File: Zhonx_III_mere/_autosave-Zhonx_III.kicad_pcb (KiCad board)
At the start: 2 copper layers, 70 x 97 mm, 133 parts, among them K1 L_Motor, K2 R_Motor, K3 USART, P1 JTAG, Q1 FDV301N, Q2 FDV301N, U1 MCP73213, U10 BSL214N, U11 BSL214N, U12 24LC64T, U14 STM32F405RGT6, U16 Line_1, U17 Line_2, U18 Line_3, U19 Line_4, U2 A3918, U20 Line_5, U3 A3918, U4 LTC2955CTS8-2, U5 SIB911DK, U6 SI1551DL, U7 LM2940, U8 MCP1700, U9 MCP1700, X1 16MHz

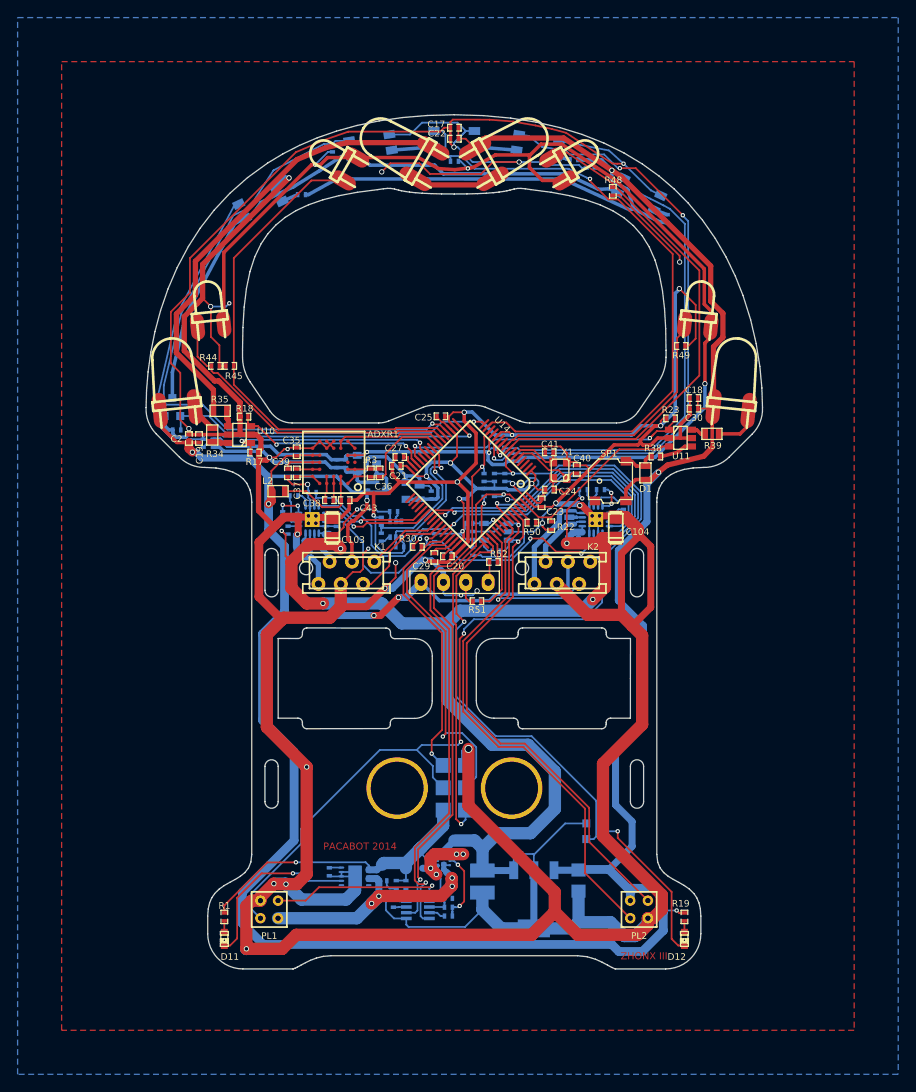
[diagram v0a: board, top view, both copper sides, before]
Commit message: Create Zhonx mere V2
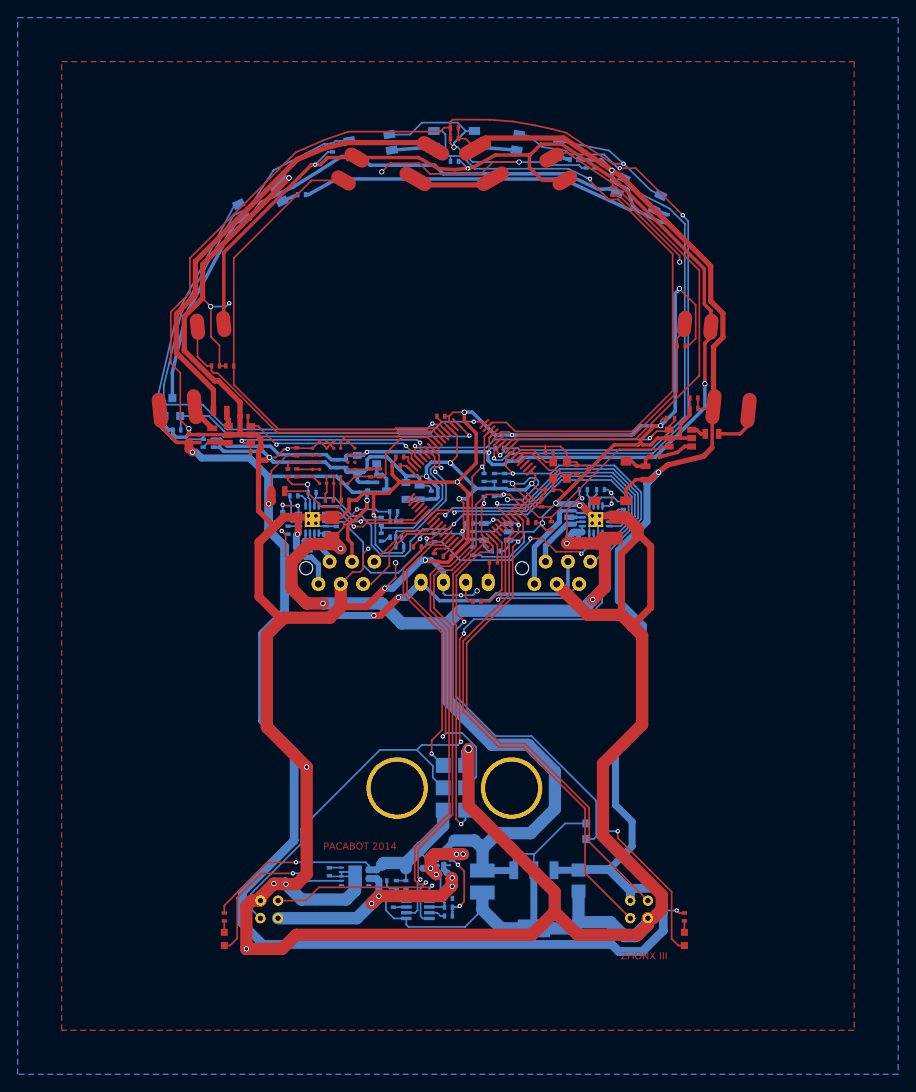
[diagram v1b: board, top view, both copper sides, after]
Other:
- board outline removed

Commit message: Nouvelle librairie (.pretty)
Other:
- board outline added: 70 x 97 mm
